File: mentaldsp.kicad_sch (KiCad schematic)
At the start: 10 parts, among them J1 NEMA Conn, J2 NEMA Conn, J3 NEMA Conn, J4 NEMA Conn, U1 TMC2209_Node0, U2 ESP32-S3-DevKitC, U3 TMC2209_Node1, U4 TMC2209_Node2, U5 TMC2209_Node3

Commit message: basic routing
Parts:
- added J6: Barrel_Jack_Switch, lib_footprint:Generic_PowerJack, symbol Connector:Barrel_Jack_Switch
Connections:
- net +12V: now also J6.2
- net DIAG0: now also U2.20 (GPIO14/ADC2_CH3); no longer U2.15 (GPIO9/ADC1_CH8)
- net DIAG1: now also U2.17 (GPIO11/ADC2_CH0); no longer U2.16 (GPIO10/ADC1_CH9)
- net DIAG2: now also U2.10 (GPIO17/ADC2_CH6); no longer U2.17 (GPIO11/ADC2_CH0)
- net DIAG3: now also U2.7 (GPIO7/ADC1_CH6); no longer U2.18 (GPIO12/ADC2_CH1)
- net DIR0: now also U2.18 (GPIO12/ADC2_CH1); no longer U2.4 (GPIO4/ADC1_CH3)
- net DIR1: now also U2.15 (GPIO9/ADC1_CH8); no longer U2.5 (GPIO5/ADC1_CH4)
- net DIR2: now also U2.8 (GPIO15/ADC2_CH4/32K_P); no longer U2.6 (GPIO6/ADC1_CH5)
- net DIR3: now also U2.4 (GPIO4/ADC1_CH3); no longer U2.7 (GPIO7/ADC1_CH6)
- net GND: now also J6.1, J6.3
- net STEP0: now also U2.19 (GPIO13/ADC2_CH2); no longer U2.8 (GPIO15/ADC2_CH4/32K_P)
- net STEP1: now also U2.16 (GPIO10/ADC1_CH9); no longer U2.9 (GPIO16/ADC2_CH5/32K_N)
- net STEP2: now also U2.9 (GPIO16/ADC2_CH5/32K_N); no longer U2.10 (GPIO17/ADC2_CH6)
- net STEP3: now also U2.5 (GPIO5/ADC1_CH4); no longer U2.11 (GPIO18/ADC2_CH7)

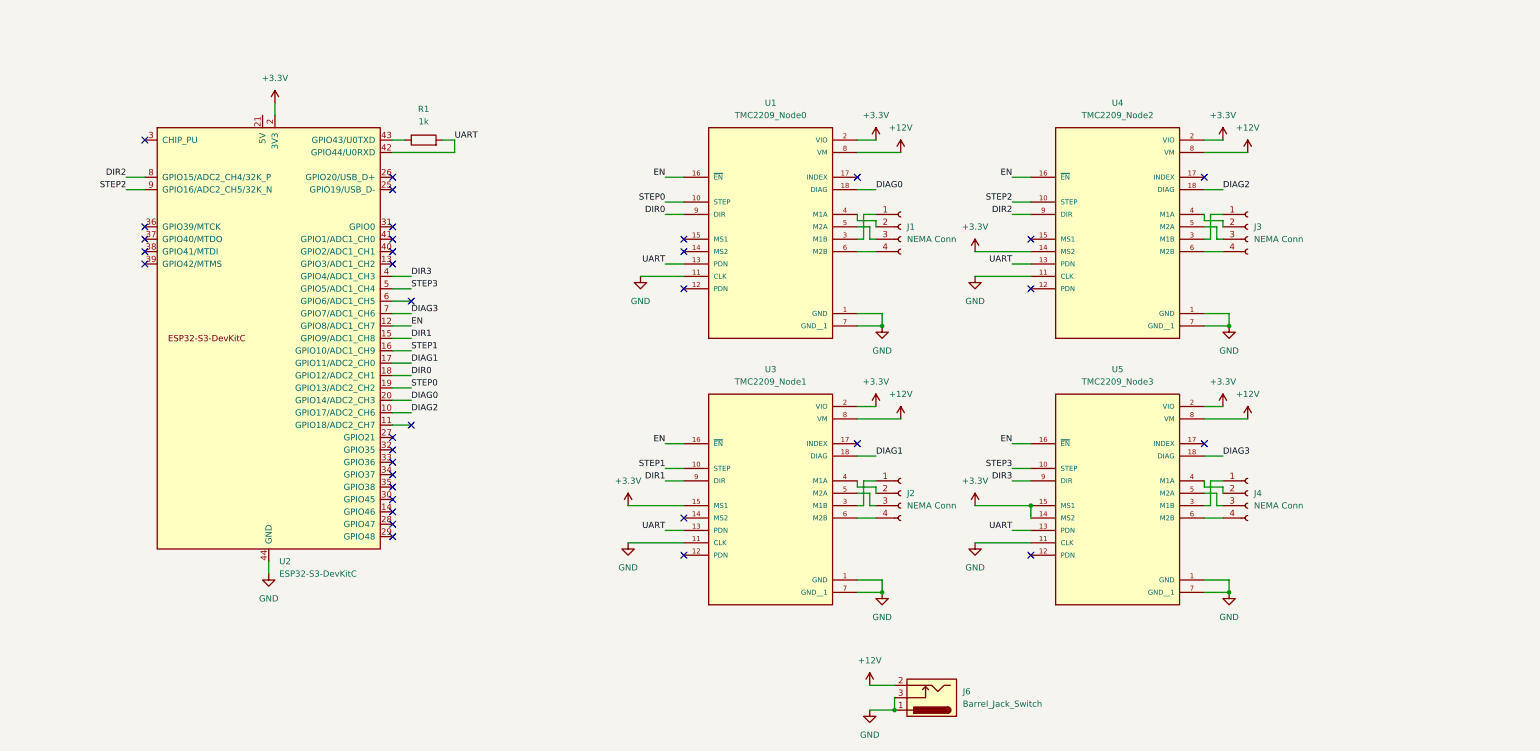
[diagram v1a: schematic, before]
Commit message: v2 with BTT TMC2209
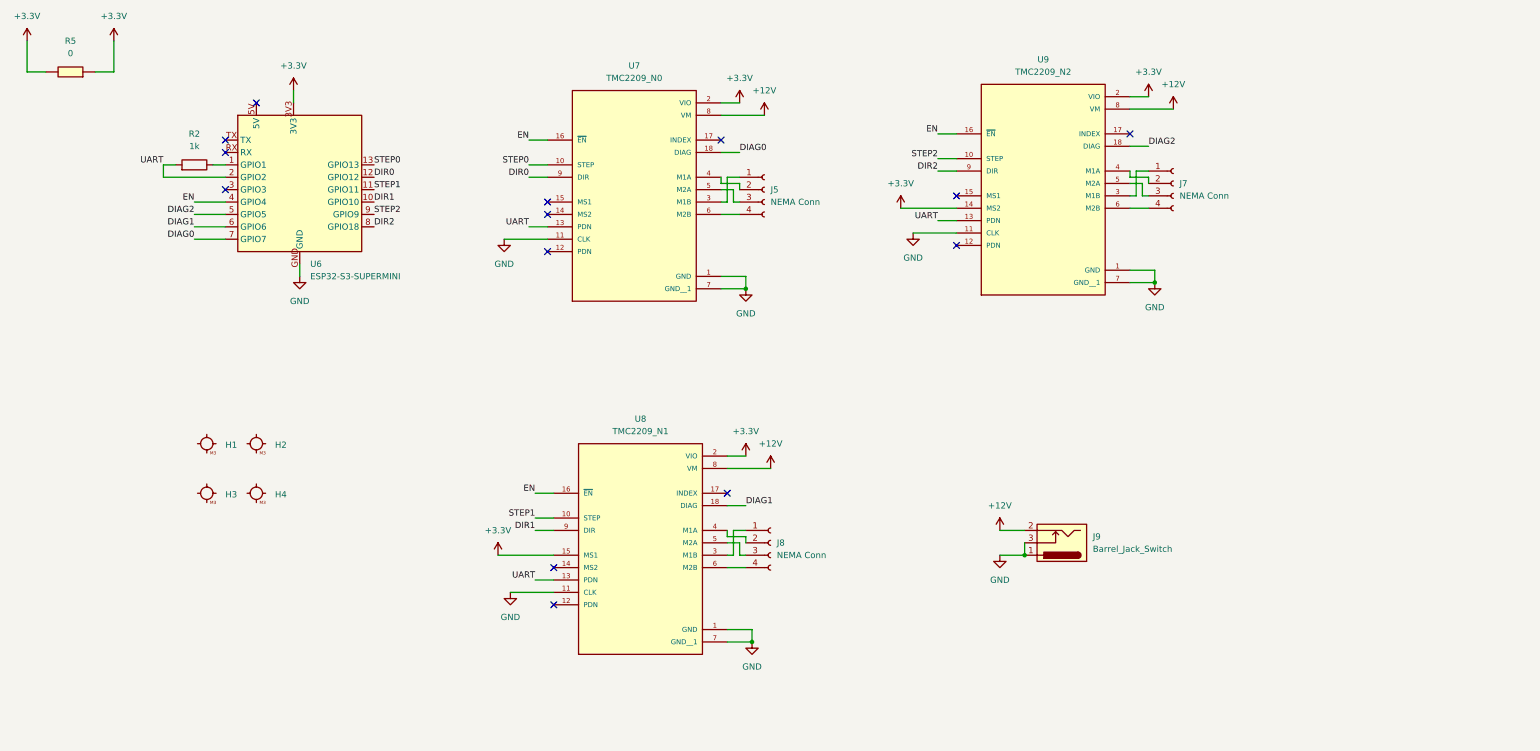
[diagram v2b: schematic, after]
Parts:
- removed J1, J2, J3, J4: NEMA Conn, Connector_PinHeader_2.54mm:PinHeader_1x04_P2.54mm_Vertical, symbol Connector:Conn_01x04_Socket
- removed J6: Barrel_Jack_Switch, lib_footprint:Generic_PowerJack, symbol Connector:Barrel_Jack_Switch
- removed R1: 1k, Resistor_SMD:R_1206_3216Metric_Pad1.30x1.75mm_HandSolder, symbol Device:R
- removed U1: TMC2209_Node0, footprints:MODULE_TMC2209_SILENTSTEPSTICK, symbol TMC2209_SILENTSTEPSTICK:TMC2209_SILENTSTEPSTICK
- removed U2: ESP32-S3-DevKitC, PCM_Espressif:ESP32-S3-DevKitC, symbol PCM_Espressif:ESP32-S3-DevKitC
- removed U3: TMC2209_Node1, footprints:MODULE_TMC2209_SILENTSTEPSTICK, symbol TMC2209_SILENTSTEPSTICK:TMC2209_SILENTSTEPSTICK
- removed U4: TMC2209_Node2, footprints:MODULE_TMC2209_SILENTSTEPSTICK, symbol TMC2209_SILENTSTEPSTICK:TMC2209_SILENTSTEPSTICK
- removed U5: TMC2209_Node3, footprints:MODULE_TMC2209_SILENTSTEPSTICK, symbol TMC2209_SILENTSTEPSTICK:TMC2209_SILENTSTEPSTICK
- added H1, H2, H3, H4: (no value), PCM_fab:MountingHole_M3, symbol PCM_fab:MountingHole_M3
- added J5, J7, J8: NEMA Conn, Connector_PinHeader_2.54mm:PinHeader_1x04_P2.54mm_Vertical, symbol Connector:Conn_01x04_Socket
- added J9: Barrel_Jack_Switch, lib_footprint:Generic_PowerJack, symbol Connector:Barrel_Jack_Switch
- added R2: 1k, PCM_fab:R_1206, symbol Device:R
- added R5: 0, PCM_fab:R_1206, symbol PCM_fab:R_1206
- added U6: ESP32-S3-SUPERMINI, lib_footprint:ESP32-S3-SuperMini, symbol lib_symbol:ESP32-S3-SUPERMINI
- added U7: TMC2209_N0, lib_footprint:BTT_TMC2209, symbol lib_symbol:TMC2209_SILENTSTEPSTICK
- added U8: TMC2209_N1, lib_footprint:BTT_TMC2209, symbol lib_symbol:TMC2209_SILENTSTEPSTICK
- added U9: TMC2209_N2, lib_footprint:BTT_TMC2209, symbol lib_symbol:TMC2209_SILENTSTEPSTICK
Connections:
- net +12V: now also J9.2, U7.8 (VM), U8.8 (VM), U9.8 (VM)
- net +3.3V: now also R5.1, R5.2, U6.3V3, U7.2 (VIO), U8.15 (MS1), U8.2 (VIO), U9.14 (MS2), U9.2 (VIO)
- net DIAG0: now also U6.7 (GPIO7), U7.18 (DIAG)
- net DIAG1: now also U6.6 (GPIO6), U8.18 (DIAG)
- net DIAG2: now also U6.5 (GPIO5), U9.18 (DIAG)
- net DIR0: now also U6.12 (GPIO12), U7.9 (DIR)
- net DIR1: now also U6.10 (GPIO10), U8.9 (DIR)
- net DIR2: now also U6.8 (GPIO18), U9.9 (DIR)
- net EN: now also U6.4 (GPIO4), U7.16 (~{EN}), U8.16 (~{EN}), U9.16 (~{EN})
- net GND: now also J9.1, J9.3, U6.GND, U7.1 (GND), U7.11 (CLK), U7.7 (GND__1), U8.1 (GND), U8.11 (CLK), U8.7 (GND__1), U9.1 (GND), U9.11 (CLK), U9.7 (GND__1)
- net STEP0: now also U6.13 (GPIO13), U7.10 (STEP)
- net STEP1: now also U6.11 (GPIO11), U8.10 (STEP)
- net STEP2: now also U6.9 (GPIO9), U9.10 (STEP)
- net UART: now also R2.2, U6.2 (GPIO2), U7.13 (PDN), U8.13 (PDN), U9.13 (PDN)
- new net: J7.1 (Pin_1), U9.3 (M1B)
- new net: J7.2 (Pin_2), U9.4 (M1A)
- new net: J7.3 (Pin_3), U9.5 (M2A)
- new net: J7.4 (Pin_4), U9.6 (M2B)
- new net: R2.1, U6.1 (GPIO1)
- new net: J8.1 (Pin_1), U8.3 (M1B)
- new net: J8.2 (Pin_2), U8.4 (M1A)
- new net: J8.3 (Pin_3), U8.5 (M2A)
- new net: J8.4 (Pin_4), U8.6 (M2B)
- new net: J5.1 (Pin_1), U7.3 (M1B)
- new net: J5.2 (Pin_2), U7.4 (M1A)
- new net: J5.3 (Pin_3), U7.5 (M2A)
- new net: J5.4 (Pin_4), U7.6 (M2B)
- no-connect marks 34 -> 14

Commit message: decoupling
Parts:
- added C1, C10, C12, C2, C3, C4, C6, C8: 100n, PCM_fab:C_1206, symbol PCM_fab:C_1206
- added C11, C5, C7, C9: 10u, PCM_fab:C_1206, symbol PCM_fab:C_1206
- added C13: 220u, PCM_fab:CP_Elec_100uF_Panasonic_EEE-FN1E101UL, symbol PCM_fab:CP_Elec_100uF_Panasonic_EEE-FN1E101UL
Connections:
- net +12V: now also C10.2, C11.2, C12.1, C13.1, C6.2, C7.2, C8.2, C9.2
- net +3.3V: now also C1.2, C2.2, C3.2, C4.2, C5.2
- net GND: now also C1.1, C10.1, C11.1, C12.2, C13.2, C2.1, C3.1, C4.1, C5.1, C6.1, C7.1, C8.1, C9.1
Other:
- moved on the sheet: J9

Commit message: cleanup
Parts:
- added R6: 10k, PCM_fab:R_1206, symbol PCM_fab:R_1206
- added R7, R8: 0, PCM_fab:R_1206, symbol PCM_fab:R_1206
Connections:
- net +3.3V: now also U8.14 (MS2), U9.15 (MS1), R6.2; no longer U8.15 (MS1), U9.14 (MS2)
- net EN: now also R6.1
- net GND: now also U7.14 (MS2), U7.15 (MS1), U8.15 (MS1), U9.14 (MS2), R7.1, R7.2, R8.1, R8.2
- no-connect marks 14 -> 10

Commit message: cleanup2
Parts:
- U8: value TMC2209_N1 -> TMC2209_N2
- U9: value TMC2209_N2 -> TMC2209_N1
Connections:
- net DIAG1: now also U6.5 (GPIO5), U9.18 (DIAG); no longer U6.6 (GPIO6), U8.18 (DIAG)
- net DIAG2: now also U6.6 (GPIO6), U8.18 (DIAG); no longer U6.5 (GPIO5), U9.18 (DIAG)
- net DIR1: now also U6.8 (GPIO18), U9.9 (DIR); no longer U6.10 (GPIO10), U8.9 (DIR)
- net DIR2: now also U6.10 (GPIO10), U8.9 (DIR); no longer U6.8 (GPIO18), U9.9 (DIR)
- net STEP1: now also U6.9 (GPIO9), U9.10 (STEP); no longer U6.11 (GPIO11), U8.10 (STEP)
- net STEP2: now also U6.11 (GPIO11), U8.10 (STEP); no longer U6.9 (GPIO9), U9.10 (STEP)
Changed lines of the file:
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@@
 		)
 	)
-	(label "DIR1"
+	(label "DIR2"
 		(at 128.27 123.19 180)
 		(effects
@@
 		)
 	)
-	(label "DIAG1"
+	(label "DIAG2"
 		(at 171.45 118.11 0)
 		(effects
@@
 		)
 	)
-	(label "DIAG2"
+	(label "DIAG1"
 		(at 58.42 58.42 180)
 		(effects
@@
 		)
 	)
-	(label "DIR2"
+	(label "DIR1"
 		(at 210.82 49.53 180)
 		(effects
@@
 		)
 	)
-	(label "DIR1"
+	(label "DIR2"
 		(at 95.25 55.88 0)
 		(effects
@@
 		)
 	)
-	(label "STEP2"
+	(label "STEP1"
 		(at 95.25 58.42 0)
 		(effects
@@
 		)
 	)
-	(label "STEP2"
+	(label "STEP1"
 		(at 210.82 46.99 180)
 		(effects
@@
 		)
 	)
-	(label "DIAG2"
+	(label "DIAG1"
 		(at 254 44.45 0)
 		(effects
@@
 		)
 	)
-	(label "STEP1"
+	(label "STEP2"
 		(at 95.25 53.34 0)
 		(effects
@@
 		)
 	)
-	(label "DIR2"
+	(label "DIR1"
 		(at 95.25 60.96 0)
 		(effects
@@
 		)
 	)
-	(label "DIAG1"
+	(label "DIAG2"
 		(at 58.42 60.96 180)
 		(effects
@@
 		)
 	)
-	(label "STEP1"
+	(label "STEP2"
 		(at 128.27 120.65 180)
 		(effects
@@
 			)
 		)
-		(property "Value" "TMC2209_N2"
+		(property "Value" "TMC2209_N1"
 			(at 232.41 29.21 0)
 			(show_name no)
@@
 			)
 		)
-		(property "Value" "TMC2209_N1"
+		(property "Value" "TMC2209_N2"
 			(at 149.86 102.87 0)
 			(show_name no)

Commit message: gerber
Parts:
- C1, C10, C11, C12, C2, C3, C4, C5, C6, C7, C8, C9: footprint PCM_fab:C_1206 -> Capacitor_SMD:C_1206_3216Metric
- R2, R5, R6, R7, R8: footprint PCM_fab:R_1206 -> Resistor_SMD:R_1206_3216Metric
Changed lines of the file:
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@@
 			)
 		)
-		(property "Footprint" "PCM_fab:C_1206"
+		(property "Footprint" "Capacitor_SMD:C_1206_3216Metric"
 			(at 179.07 41.91 0)
 			(hide yes)
@@
 			)
 		)
-		(property "Footprint" "PCM_fab:C_1206"
+		(property "Footprint" "Capacitor_SMD:C_1206_3216Metric"
 			(at 190.5 41.91 0)
 			(hide yes)
@@
 			)
 		)
-		(property "Footprint" "PCM_fab:C_1206"
+		(property "Footprint" "Capacitor_SMD:C_1206_3216Metric"
 			(at 275.59 40.64 0)
 			(hide yes)
@@
 			)
 		)
-		(property "Footprint" "PCM_fab:C_1206"
+		(property "Footprint" "Capacitor_SMD:C_1206_3216Metric"
 			(at 100.33 36.83 0)
 			(hide yes)
@@
 			)
 		)
-		(property "Footprint" "PCM_fab:C_1206"
+		(property "Footprint" "Capacitor_SMD:C_1206_3216Metric"
 			(at 111.76 36.83 0)
 			(hide yes)
@@
 			)
 		)
-		(property "Footprint" "PCM_fab:C_1206"
+		(property "Footprint" "Capacitor_SMD:C_1206_3216Metric"
 			(at 184.15 114.3 0)
 			(hide yes)
@@
 			)
 		)
-		(property "Footprint" "PCM_fab:C_1206"
+		(property "Footprint" "Capacitor_SMD:C_1206_3216Metric"
 			(at 195.58 114.3 0)
 			(hide yes)
@@
 			)
 		)
-		(property "Footprint" "PCM_fab:R_1206"
+		(property "Footprint" "Resistor_SMD:R_1206_3216Metric"
 			(at 33.02 29.21 90)
 			(hide yes)
@@
 			)
 		)
-		(property "Footprint" "PCM_fab:C_1206"
+		(property "Footprint" "Capacitor_SMD:C_1206_3216Metric"
 			(at 233.68 147.32 0)
 			(hide yes)
@@
 			)
 		)
-		(property "Footprint" "PCM_fab:C_1206"
+		(property "Footprint" "Capacitor_SMD:C_1206_3216Metric"
 			(at 254 30.48 0)
 			(hide yes)
@@
 			)
 		)
-		(property "Footprint" "PCM_fab:C_1206"
+		(property "Footprint" "Capacitor_SMD:C_1206_3216Metric"
 			(at 170.18 31.75 0)
 			(hide yes)
@@
 			)
 		)
-		(property "Footprint" "PCM_fab:C_1206"
+		(property "Footprint" "Capacitor_SMD:C_1206_3216Metric"
 			(at 264.16 40.64 0)
 			(hide yes)
@@
 			)
 		)
-		(property "Footprint" "PCM_fab:R_1206"
+		(property "Footprint" "Resistor_SMD:R_1206_3216Metric"
 			(at 58.42 50.038 90)
 			(hide yes)
@@
 			)
 		)
-		(property "Footprint" "PCM_fab:R_1206"
+		(property "Footprint" "Resistor_SMD:R_1206_3216Metric"
 			(at 33.02 45.72 90)
 			(hide yes)
@@
 			)
 		)
-		(property "Footprint" "PCM_fab:C_1206"
+		(property "Footprint" "Capacitor_SMD:C_1206_3216Metric"
 			(at 171.45 104.14 0)
 			(hide yes)
@@
 			)
 		)
-		(property "Footprint" "PCM_fab:R_1206"
+		(property "Footprint" "Resistor_SMD:R_1206_3216Metric"
 			(at 33.02 63.5 90)
 			(hide yes)
@@
 			)
 		)
-		(property "Footprint" "PCM_fab:R_1206"
+		(property "Footprint" "Resistor_SMD:R_1206_3216Metric"
 			(at 33.02 54.61 90)
 			(hide yes)

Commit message: replace to SMD jack
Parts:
- removed J9: Barrel_Jack_Switch, lib_footprint:Generic_PowerJack, symbol Connector:Barrel_Jack_Switch
- added J1: Conn_PWRJack_2x5.5mm_CUIDevices_PJ-002AH-SMT-TR, PCM_fab:CUIDevices_PJ-002AH-SMT-TR_PWRJack_2x5.5mm, symbol PCM_fab:Conn_PWRJack_2x5.5mm_CUIDevices_PJ-002AH-SMT-TR
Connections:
- net +12V: now also J1.2
- net GND: now also J1.1, J1.3
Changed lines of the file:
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@@
 	)
 	(junction
+		(at 252.73 148.59)
+		(diameter 0)
+		(color 0 0 0 0)
+	)
+	(junction
 		(at 184.15 110.49)
 		(diameter 0)
@@
 	)
 	(junction
-		(at 252.73 148.59)
-		(diameter 0)
-		(color 0 0 0 0)
-	)
-	(junction
 		(at 233.68 151.13)
 		(diameter 0)
@@
 	(wire
 		(pts
-			(xy 252.73 151.13) (xy 252.73 148.59)
+			(xy 64.77 50.8) (xy 52.07 50.8)
 		)
 		(stroke
@@
 	(wire
 		(pts
-			(xy 64.77 50.8) (xy 52.07 50.8)
+			(xy 252.73 146.05) (xy 252.73 148.59)
 		)
 		(stroke
@@
 	(wire
 		(pts
-			(xy 252.73 146.05) (xy 252.73 148.59)
-		)
-		(stroke
-			(width 0)
-			(type default)
-		)
-	)
-	(wire
-		(pts
 			(xy 113.03 130.81) (xy 132.08 130.81)
 		)
@@
 	(wire
 		(pts
+			(xy 252.73 148.59) (xy 252.73 151.13)
+		)
+		(stroke
+			(width 0)
+			(type default)
+		)
+	)
+	(wire
+		(pts
 			(xy 130.81 55.88) (xy 130.81 58.42)
 		)
@@
 	)
 	(symbol
-		(lib_id "PCM_fab:C_1206")
-		(at 171.45 104.14 0)
+		(lib_id "PCM_fab:Conn_PWRJack_2x5.5mm_CUIDevices_PJ-002AH-SMT-TR")
+		(at 260.35 146.05 180)
 		(unit 1)
 		(body_style 1)
@@
 		(dnp no)
 		(fields_autoplaced yes)
-		(property "Reference" "C3"
-			(at 175.26 102.8699 0)
+		(property "Reference" "J1"
+			(at 266.7 144.7799 0)
 			(show_name no)
 			(do_not_autoplace no)
@@
 					(size 1.27 1.27)
 				)
-				(justify left)
+				(justify right)
 			)
 		)
-		(property "Value" "100n"
-			(at 175.26 105.4099 0)
+		(property "Value" "Conn_PWRJack_2x5.5mm_CUIDevices_PJ-002AH-SMT-TR"
+			(at 266.7 147.3199 0)
 			(show_name no)
 			(do_not_autoplace no)
@@
 					(size 1.27 1.27)
 				)
-				(justify left)
+				(justify right)
 			)
 		)
-		(property "Footprint" "Capacitor_SMD:C_1206_3216Metric"
-			(at 171.45 104.14 0)
+		(property "Footprint" "PCM_fab:CUIDevices_PJ-002AH-SMT-TR_PWRJack_2x5.5mm"
+			(at 259.08 145.034 0)
 			(hide yes)
 			(show_name no)
@@
 			)
 		)
-		(property "Datasheet" "https://www.yageo.com/upload/media/product/productsearch/datasheet/mlcc/UPY-GP_NP0_16V-to-50V_18.pdf"
-			(at 171.45 104.14 0)
+		(property "Datasheet" "https://www.cuidevices.com/product/resource/pj-002ah-smt-tr.pdf"
+			(at 259.08 145.034 0)
 			(hide yes)
 			(show_name no)
@@
 			)
 		)
-		(property "Description" "Unpolarized capacitor, SMD, 1206"
-			(at 171.45 104.14 0)
+		(property "Description" "Power Barrel Connector Jack 2.00mm ID (0.079\"), 5.50mm OD (0.217\") Surface Mount"
+			(at 260.35 146.05 0)
 			(hide yes)
 			(show_name no)
@@
 		(pin "2"
 		)
+		(pin "3"
+		)
 		(instances
 			(project "mentaldsp"
 				(path "/77e5f02d-709f-44d0-a9cf-86ffbae129e9"
-					(reference "C3")
+					(reference "J1")
 					(unit 1)
 				)
@@
 	)
 	(symbol
-		(lib_id "Connector:Barrel_Jack_Switch")
-		(at 260.35 146.05 180)
+		(lib_id "PCM_fab:C_1206")
+		(at 171.45 104.14 0)
 		(unit 1)
 		(body_style 1)
@@
 		(dnp no)
 		(fields_autoplaced yes)
-		(property "Reference" "J9"
-			(at 266.7 144.7799 0)
+		(property "Reference" "C3"
+			(at 175.26 102.8699 0)
 			(show_name no)
 			(do_not_autoplace no)
@@
 					(size 1.27 1.27)
 				)
-				(justify right)
+				(justify left)
 			)
 		)
-		(property "Value" "Barrel_Jack_Switch"
-			(at 266.7 147.3199 0)
+		(property "Value" "100n"
+			(at 175.26 105.4099 0)
 			(show_name no)
 			(do_not_autoplace no)
@@
 					(size 1.27 1.27)
 				)
-				(justify right)
+				(justify left)
 			)
 		)
-		(property "Footprint" "lib_footprint:Generic_PowerJack"
-			(at 259.08 145.034 0)
+		(property "Footprint" "Capacitor_SMD:C_1206_3216Metric"
+			(at 171.45 104.14 0)
 			(hide yes)
 			(show_name no)
@@
 			)
 		)
-		(property "Datasheet" ""
-			(at 259.08 145.034 0)
+		(property "Datasheet" "https://www.yageo.com/upload/media/product/productsearch/datasheet/mlcc/UPY-GP_NP0_16V-to-50V_18.pdf"
+			(at 171.45 104.14 0)
 			(hide yes)
 			(show_name no)
@@
 			)
 		)
-		(property "Description" "DC Barrel Jack with an internal switch"
-			(at 260.35 146.05 0)
+		(property "Description" "Unpolarized capacitor, SMD, 1206"
+			(at 171.45 104.14 0)
 			(hide yes)
 			(show_name no)
@@
 		(pin "2"
 		)
-		(pin "3"
-		)
 		(instances
 			(project "mentaldsp"
 				(path "/77e5f02d-709f-44d0-a9cf-86ffbae129e9"
-					(reference "J9")
+					(reference "C3")
 					(unit 1)
 				)

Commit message: fix polarity
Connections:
- net +12V: now also J1.3
- net GND: no longer J1.3
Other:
- moved on the sheet: J1
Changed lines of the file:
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@@
 	)
 	(junction
-		(at 233.68 143.51)
+		(at 252.73 143.51)
 		(diameter 0)
 		(color 0 0 0 0)
 	)
 	(junction
-		(at 179.07 38.1)
+		(at 233.68 143.51)
 		(diameter 0)
 		(color 0 0 0 0)
 	)
 	(junction
-		(at 171.45 107.95)
+		(at 179.07 38.1)
 		(diameter 0)
 		(color 0 0 0 0)
 	)
 	(junction
-		(at 252.73 148.59)
+		(at 171.45 107.95)
 		(diameter 0)
 		(color 0 0 0 0)
@@
 	(wire
 		(pts
-			(xy 252.73 146.05) (xy 252.73 148.59)
-		)
-		(stroke
-			(width 0)
-			(type default)
-		)
-	)
-	(wire
-		(pts
 			(xy 166.37 73.66) (xy 171.45 73.66)
 		)
@@
 	(wire
 		(pts
+			(xy 256.54 146.05) (xy 252.73 146.05)
+		)
+		(stroke
+			(width 0)
+			(type default)
+		)
+	)
+	(wire
+		(pts
 			(xy 58.42 58.42) (xy 64.77 58.42)
 		)
@@
 	(wire
 		(pts
+			(xy 252.73 143.51) (xy 256.54 143.51)
+		)
+		(stroke
+			(width 0)
+			(type default)
+		)
+	)
+	(wire
+		(pts
 			(xy 113.03 130.81) (xy 132.08 130.81)
 		)
@@
 	(wire
 		(pts
+			(xy 256.54 148.59) (xy 252.73 148.59)
+		)
+		(stroke
+			(width 0)
+			(type default)
+		)
+	)
+	(wire
+		(pts
 			(xy 167.64 130.81) (xy 171.45 130.81)
 		)
@@
 	(wire
 		(pts
+			(xy 252.73 146.05) (xy 252.73 143.51)
+		)
+		(stroke
+			(width 0)
+			(type default)
+		)
+	)
+	(wire
+		(pts
 			(xy 41.91 63.5) (xy 41.91 67.31)
 		)
@@
 	(symbol
 		(lib_id "PCM_fab:Conn_PWRJack_2x5.5mm_CUIDevices_PJ-002AH-SMT-TR")
-		(at 260.35 146.05 180)
+		(at 264.16 146.05 180)
 		(unit 1)
 		(body_style 1)
@@
 		(fields_autoplaced yes)
 		(property "Reference" "J1"
-			(at 266.7 144.7799 0)
+			(at 270.51 144.7799 0)
 			(show_name no)
 			(do_not_autoplace no)
@@
 		)
 		(property "Value" "Conn_PWRJack_2x5.5mm_CUIDevices_PJ-002AH-SMT-TR"
-			(at 266.7 147.3199 0)
+			(at 270.51 147.3199 0)
 			(show_name no)
 			(do_not_autoplace no)
@@
 		)
 		(property "Footprint" "PCM_fab:CUIDevices_PJ-002AH-SMT-TR_PWRJack_2x5.5mm"
-			(at 259.08 145.034 0)
+			(at 262.89 145.034 0)
 			(hide yes)
 			(show_name no)
@@
 		)
 		(property "Datasheet" "https://www.cuidevices.com/product/resource/pj-002ah-smt-tr.pdf"
-			(at 259.08 145.034 0)
+			(at 262.89 145.034 0)
 			(hide yes)
 			(show_name no)
@@
 		)
 		(property "Description" "Power Barrel Connector Jack 2.00mm ID (0.079\"), 5.50mm OD (0.217\") Surface Mount"
-			(at 260.35 146.05 0)
+			(at 264.16 146.05 0)
 			(hide yes)
 			(show_name no)
